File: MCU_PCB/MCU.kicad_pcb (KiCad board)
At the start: 4 copper layers, 66.8 x 87.1 mm, 30 parts, among them J1 Conn_01x06_Socket, J2 Conn_01x06_Socket, J3 Conn_01x02, J5 Conn_01x02_Pin, M1 MountingHole, M3_1 MountingHole, M3_2 MountingHole, U1 ESP32-DEVKIT-C, U2 TJA1050T/CM,118, U4 TPS54560BQDDARQ1

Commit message: updated Julias IMU to use the revised buck converter and connectors. made the back plane mostly a ground plane (for the buck converter)
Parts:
- renumbered J3 to J1, J1 to J3, U4 to U1, U1 to U3

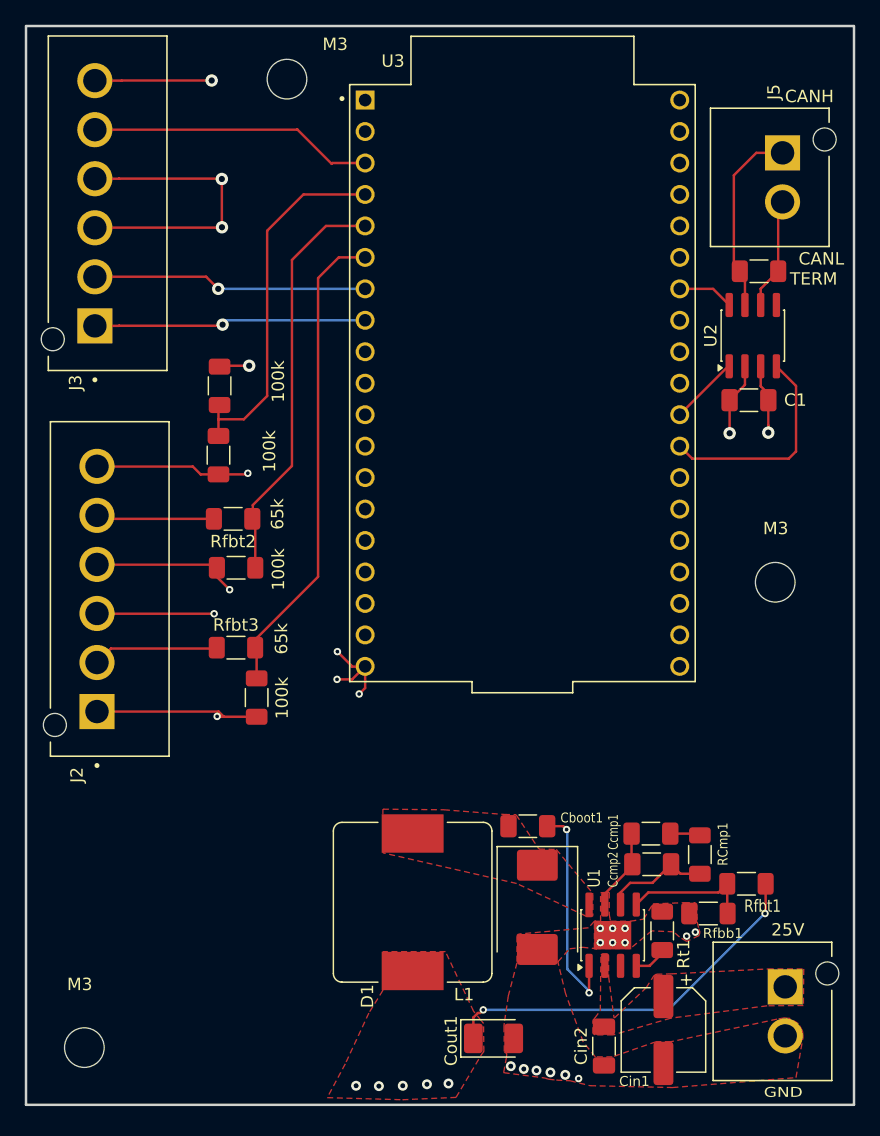
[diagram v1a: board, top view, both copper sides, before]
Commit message: small updates to buck, fixed vias, and remove connection to input connector ground pad
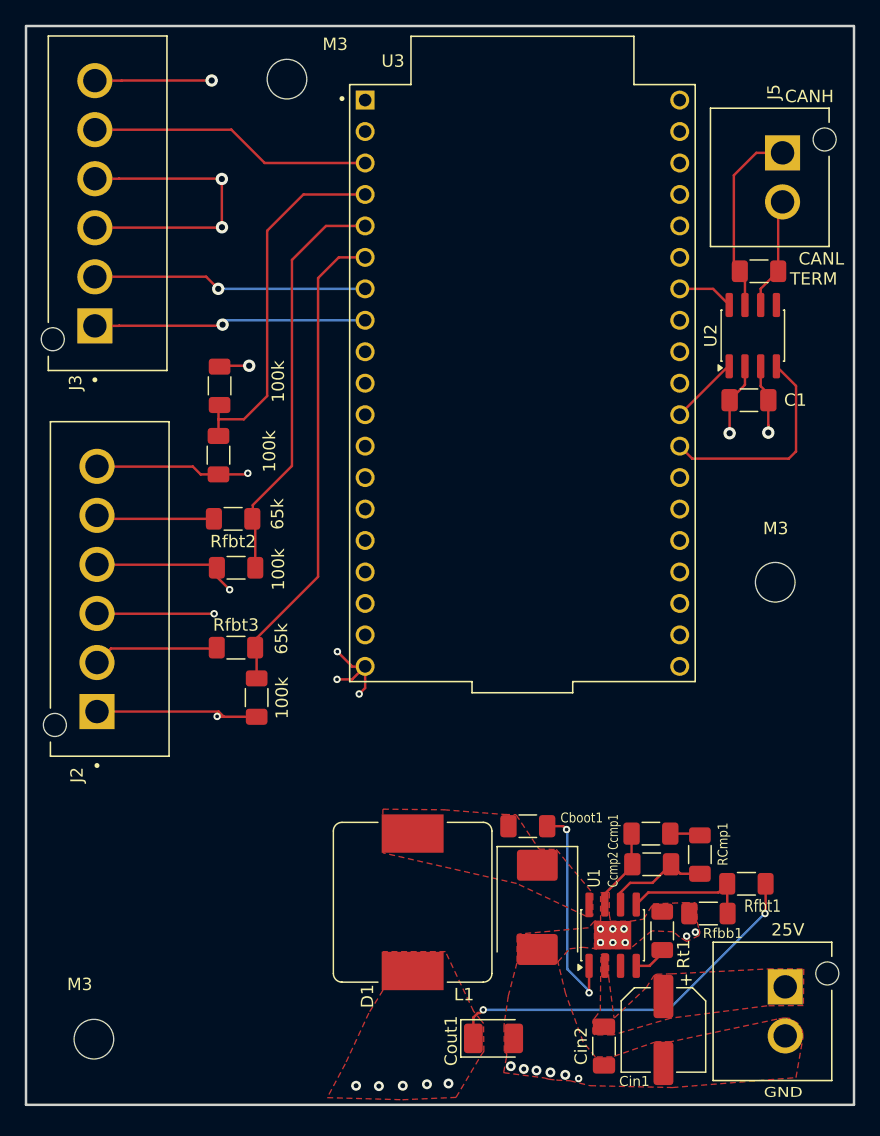
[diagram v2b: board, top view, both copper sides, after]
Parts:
- moved M1 1.03 mm to (66.3, 119.3)

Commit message: sry forgot to push, waiting on PCB shipping atm. Notes: split power distribution into two boards, one for the main 25V distribution, and another for 12V stuff. Also updated CAN transciever. the previous one was a 5V logic one (same logic as its power), and would have fried our ESPs data pins
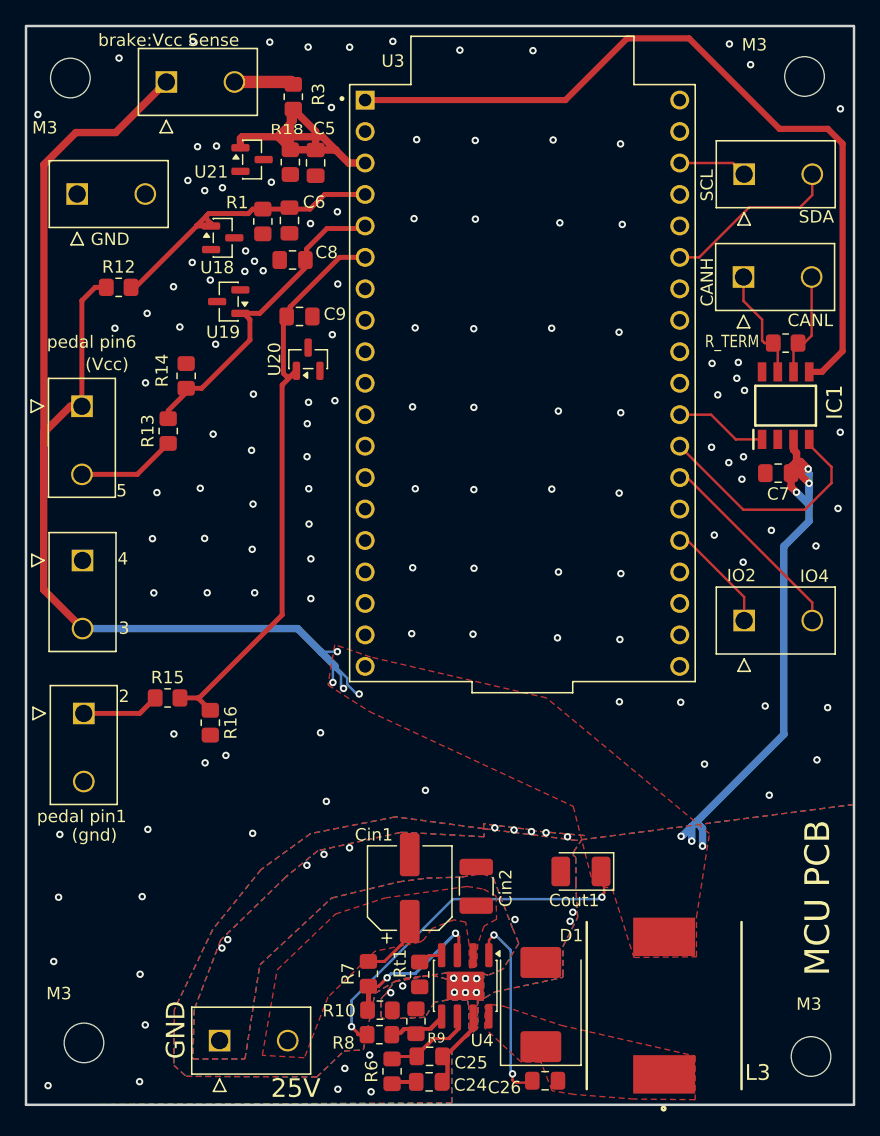
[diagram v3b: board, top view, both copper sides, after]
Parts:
- removed C1: 0.1u, Capacitor_SMD:C_1206_3216Metric_Pad1.33x1.80mm_HandSolder
- removed Cboot1: 100nF, Capacitor_SMD:C_1206_3216Metric_Pad1.33x1.80mm_HandSolder
- removed Ccmp1: 10nF, Capacitor_SMD:C_1206_3216Metric_Pad1.33x1.80mm_HandSolder
- removed Ccmp2: 10pF, Capacitor_SMD:C_1206_3216Metric_Pad1.33x1.80mm_HandSolder
- removed J1: Conn_01x02, PROVE-footprints:TE_1877285-2
- removed J2, J3: Conn_01x06_Socket, PROVE-footprints:TE_1877285-6
- removed L1: 22uH, Inductor_SMD:L_Bourns_SRP1245A
- removed R2, R4, R5: 100k, Resistor_SMD:R_1206_3216Metric_Pad1.30x1.75mm_HandSolder
- removed RCmp1: 18.2kOhm, Resistor_SMD:R_1206_3216Metric_Pad1.30x1.75mm_HandSolder
- removed Rfbb1: 11.8kOhm, Resistor_SMD:R_1206_3216Metric_Pad1.30x1.75mm_HandSolder
- removed Rfbt1, Rfbt2, Rfbt3: 64.9kOhm, Resistor_SMD:R_1206_3216Metric_Pad1.30x1.75mm_HandSolder
- removed U1: TPS54560BQDDARQ1, Package_SO:SOIC-8-1EP_3.9x4.9mm_P1.27mm_EP2.29x3mm
- removed U2: TJA1050T/CM,118, Package_SO:SOIC-8_3.9x4.9mm_P1.27mm
- added C24: 10nF, Capacitor_SMD:C_0805_2012Metric_Pad1.18x1.45mm_HandSolder, F.Cu at (93.4, 122.7)
- added C25: 10pF, Capacitor_SMD:C_0805_2012Metric_Pad1.18x1.45mm_HandSolder, F.Cu at (93.4, 120.7)
- added C26: 100nF, Capacitor_SMD:C_0805_2012Metric_Pad1.18x1.45mm_HandSolder, F.Cu at (102.7, 122.7)
- added C5: 10nF, Capacitor_SMD:C_0805_2012Metric_Pad1.18x1.45mm_HandSolder, F.Cu at (84.2, 48.5)
- added C6: 10nF, Capacitor_SMD:C_0805_2012Metric_Pad1.18x1.45mm_HandSolder, F.Cu at (82.1, 53.2)
- added C7: 100nF, Capacitor_SMD:C_0805_2012Metric_Pad1.18x1.45mm_HandSolder, F.Cu at (121.5, 73.6)
- added C8: 10nF, Capacitor_SMD:C_0805_2012Metric_Pad1.18x1.45mm_HandSolder, F.Cu at (82.3, 56.4)
- added C9: 10nF, Capacitor_SMD:C_0805_2012Metric_Pad1.18x1.45mm_HandSolder, F.Cu at (82.9, 61.0)
- added IC1: TJA1044BT/0Z, PROVE-footprints:SOIC127P600X175-8N, F.Cu at (122.2, 68.2)
- added J10: 39-28-1023, PROVE-footprints:39-28-1023, F.Cu at (118.8, 85.5)
- added J11: 39-28-1023, PROVE-footprints:39-28-1023, F.Cu at (118.8, 49.5)
- added J12: 39-28-1023, PROVE-footprints:39-28-1023, F.Cu at (76.5, 119.4)
- added J4: 39-28-1023, PROVE-footprints:39-28-1023, F.Cu at (118.8, 57.8)
- added J6: 39-28-1023, PROVE-footprints:39-28-1023, F.Cu at (65.4, 80.7)
- added J7: 39-28-1023, PROVE-footprints:39-28-1023, F.Cu at (65.5, 93.0)
- added J8: 39-28-1023, PROVE-footprints:39-28-1023, F.Cu at (72.2, 42.0)
- added J9: 39-28-1023, PROVE-footprints:39-28-1023, F.Cu at (65.0, 51.1)
- added L3: SRP1265A-220M, PROVE-footprints:SRP1265A, F.Cu at (112.3, 116.6)
- added M2: MountingHole, MountingHole:MountingHole_3.2mm_M3, F.Cu at (123.7, 41.6)
- added R1: 100k, Resistor_SMD:R_0805_2012Metric_Pad1.20x1.40mm_HandSolder, F.Cu at (79.9, 53.3)
- added R10: 38.3k, Resistor_SMD:R_0805_2012Metric_Pad1.20x1.40mm_HandSolder, F.Cu at (89.4, 117.0)
- added R12: 100k, Resistor_SMD:R_0805_2012Metric_Pad1.20x1.40mm_HandSolder, F.Cu at (68.3, 58.6)
- added R13: 64.9k, Resistor_SMD:R_0805_2012Metric_Pad1.20x1.40mm_HandSolder, F.Cu at (72.3, 70.2)
- added R14: 100k, Resistor_SMD:R_0805_2012Metric_Pad1.20x1.40mm_HandSolder, F.Cu at (73.8, 65.8)
- added R15: 64.9k, Resistor_SMD:R_0805_2012Metric_Pad1.20x1.40mm_HandSolder, F.Cu at (72.2, 91.8)
- added R16: 100k, Resistor_SMD:R_0805_2012Metric_Pad1.20x1.40mm_HandSolder, F.Cu at (75.7, 93.8)
- added R18: 100k, Resistor_SMD:R_0805_2012Metric_Pad1.20x1.40mm_HandSolder, F.Cu at (82.2, 48.5)
- added R3: 100, Resistor_SMD:R_0805_2012Metric_Pad1.20x1.40mm_HandSolder, F.Cu at (82.4, 43.2)
- added R7: 590k, Resistor_SMD:R_0805_2012Metric_Pad1.20x1.40mm_HandSolder, F.Cu at (88.5, 114.0)
- added R8: 64.9kOhm, Resistor_SMD:R_0805_2012Metric_Pad1.20x1.40mm_HandSolder, F.Cu at (89.4, 118.9)
- added R9: 11.8kOhm, Resistor_SMD:R_0805_2012Metric_Pad1.20x1.40mm_HandSolder, F.Cu at (92.3, 117.9)
- added U18: LM4040CELT-3.0, Package_TO_SOT_SMD:SOT-23, F.Cu at (76.7, 54.6)
- added U19: LM4040CELT-3.0, Package_TO_SOT_SMD:SOT-23, F.Cu at (77.2, 59.8)
- added U20: LM4040CELT-3.0, Package_TO_SOT_SMD:SOT-23, F.Cu at (83.6, 64.4)
- added U21: LM4040CELT-3.0, Package_TO_SOT_SMD:SOT-23, F.Cu at (79.1, 48.3)
- added U4: TPS54560BQDDARQ1, Package_SO:SOIC-8-1EP_3.9x4.9mm_P1.27mm_EP2.29x3mm, F.Cu at (96.3, 115.0)
- Cin2: footprint Capacitor_SMD:C_1206_3216Metric_Pad1.33x1.80mm_HandSolder -> Capacitor_SMD:C_1210_3225Metric_Pad1.33x2.70mm_HandSolder
- J5: value Conn_01x02_Pin -> 39-28-1023; footprint PROVE-footprints:TE_1877285-2 -> PROVE-footprints:39-28-1023
- R6: value 100k -> 18.2k; footprint Resistor_SMD:R_1206_3216Metric_Pad1.30x1.75mm_HandSolder -> Resistor_SMD:R_0805_2012Metric_Pad1.20x1.40mm_HandSolder
- R_TERM1, Rt1: footprint Resistor_SMD:R_1206_3216Metric_Pad1.30x1.75mm_HandSolder -> Resistor_SMD:R_0805_2012Metric_Pad1.20x1.40mm_HandSolder
- moved J5 58.5 mm to (65.3, 68.2), turned to 0 degrees
- moved M3_1 38.4 mm to (124.2, 120.7)
- moved R6 32.1 mm to (90.4, 121.9), turned to 90 degrees
- moved Cin1 23.5 mm to (91.8, 107.1), turned to 90 degrees
- moved Rt1 19.9 mm to (92.6, 114.1), turned to 90 degrees
- moved M3_2 17.5 mm to (64.4, 41.7)
- moved Cin2 16.5 mm to (97.2, 107.0), turned to -90 degrees
- moved Cout1 15.2 mm to (105.6, 105.8), turned to 180 degrees
- moved D1 7.85 mm to (102.4, 116.5), turned to 90 degrees
- moved R_TERM1 6.19 mm to (122.2, 63.1)
- moved M1 0.85 mm to (65.5, 119.6)
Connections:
- net Net-(J1-Pin_1) renamed /buck_to_5V/25V_IN
- J5 pad 1: /CANH -> 5.2V OUT
- J5 pad 2: /CANL -> /Pedal_Sense/falling_in
- R6 pad 1: Net-(U3-IO35) -> Net-(C24-Pad2)
- R6 pad 2: GND -> Net-(U4-COMP)
- U3 pad 1: unconnected-(U3-3V3-Pad1) -> /3v3
- U3 pad 14: unconnected-(U3-GND1-Pad14) -> GND
- U3 pad 24: unconnected-(U3-IO2-Pad24) -> Net-(U3-IO2)
- U3 pad 26: unconnected-(U3-IO4-Pad26) -> Net-(U3-IO4)
- U3 pad 33: unconnected-(U3-IO21-Pad33) -> Net-(U3-IO21)
- U3 pad 36: unconnected-(U3-IO22-Pad36) -> Net-(U3-IO22)
- U3 pad 4: Net-(U3-SENSOR_VN) -> /Pedal_Sense/5V_sense
- U3 pad 5: Net-(U3-IO34) -> /Pedal_Sense/falling_sense
- U3 pad 6: Net-(U3-IO35) -> /Pedal_Sense/rising_sense
- U3 pad 7: Net-(J3-Pin_2) -> unconnected-(U3-IO32-Pad7)
- U3 pad 8: Net-(J3-Pin_1) -> unconnected-(U3-IO33-Pad8)
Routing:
- net 5.2V OUT: track 76.0 -> 176.1 mm, vias 14 -> 12
- net /3v3: track 0.00 -> 64.3 mm
- net GND: track 70.8 -> 14.5 mm, vias 20 -> 146
- net /Pedal_Sense/rising_sense: track 0.00 -> 47.3 mm
- net Net-(U3-IO35): track 38.9 -> 0.00 mm
- net Net-(U3-IO34): track 33.3 -> 0.00 mm
- net Net-(U3-SENSOR_VN): track 29.7 -> 0.00 mm
- net /Pedal_Sense/falling_sense: track 0.00 -> 26.2 mm
- net /Pedal_Sense/5V_sense: track 0.00 -> 24.4 mm
- net Net-(J3-Pin_2): track 22.2 -> 0.00 mm, vias 1 -> 0
- net Net-(J3-Pin_1): track 22.0 -> 0.00 mm, vias 1 -> 0
- net Net-(U1-BOOT): track 17.8 -> 0.00 mm, vias 2 -> 0
- net Net-(U3-IO4): track 0.00 -> 16.3 mm
- net Net-(U4-BOOT): track 0.00 -> 15.6 mm, vias 0 -> 2
- net Net-(U3-IO21): track 0.00 -> 14.5 mm
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- added copper zone on B.Cu, net GND
- removed copper zone on In1.Cu, net 5.2V OUT
- removed copper zone on In2.Cu, net GND
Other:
- copper layers 4 -> 2
- board text added: "(Vcc)"
- board text added: "(gnd)"
- board text added: "2"
- board text added: "3"
- board text added: "4"
- board text added: "5"
- board text added: "IO2"
- board text added: "IO4"
- board text added: "MCU PCB"
- board text added: "R_TERM"
- board text added: "SCL"
- board text added: "SDA"
- board text added: "brake:Vcc Sense"
- board text added: "pedal pin1"
- board text added: "pedal pin6"
- board text removed: "100k"
- board text removed: "65k"
- board text removed: "TERM"
